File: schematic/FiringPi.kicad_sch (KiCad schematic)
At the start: 68 parts, among them IC1 HX711, J10 PT3, J11 PT4, J12 UART, J13 RTD0, J14 RTD1, J15 Pin, J3 Conn_01x03, J4 Conn_01x03, J5 Relay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

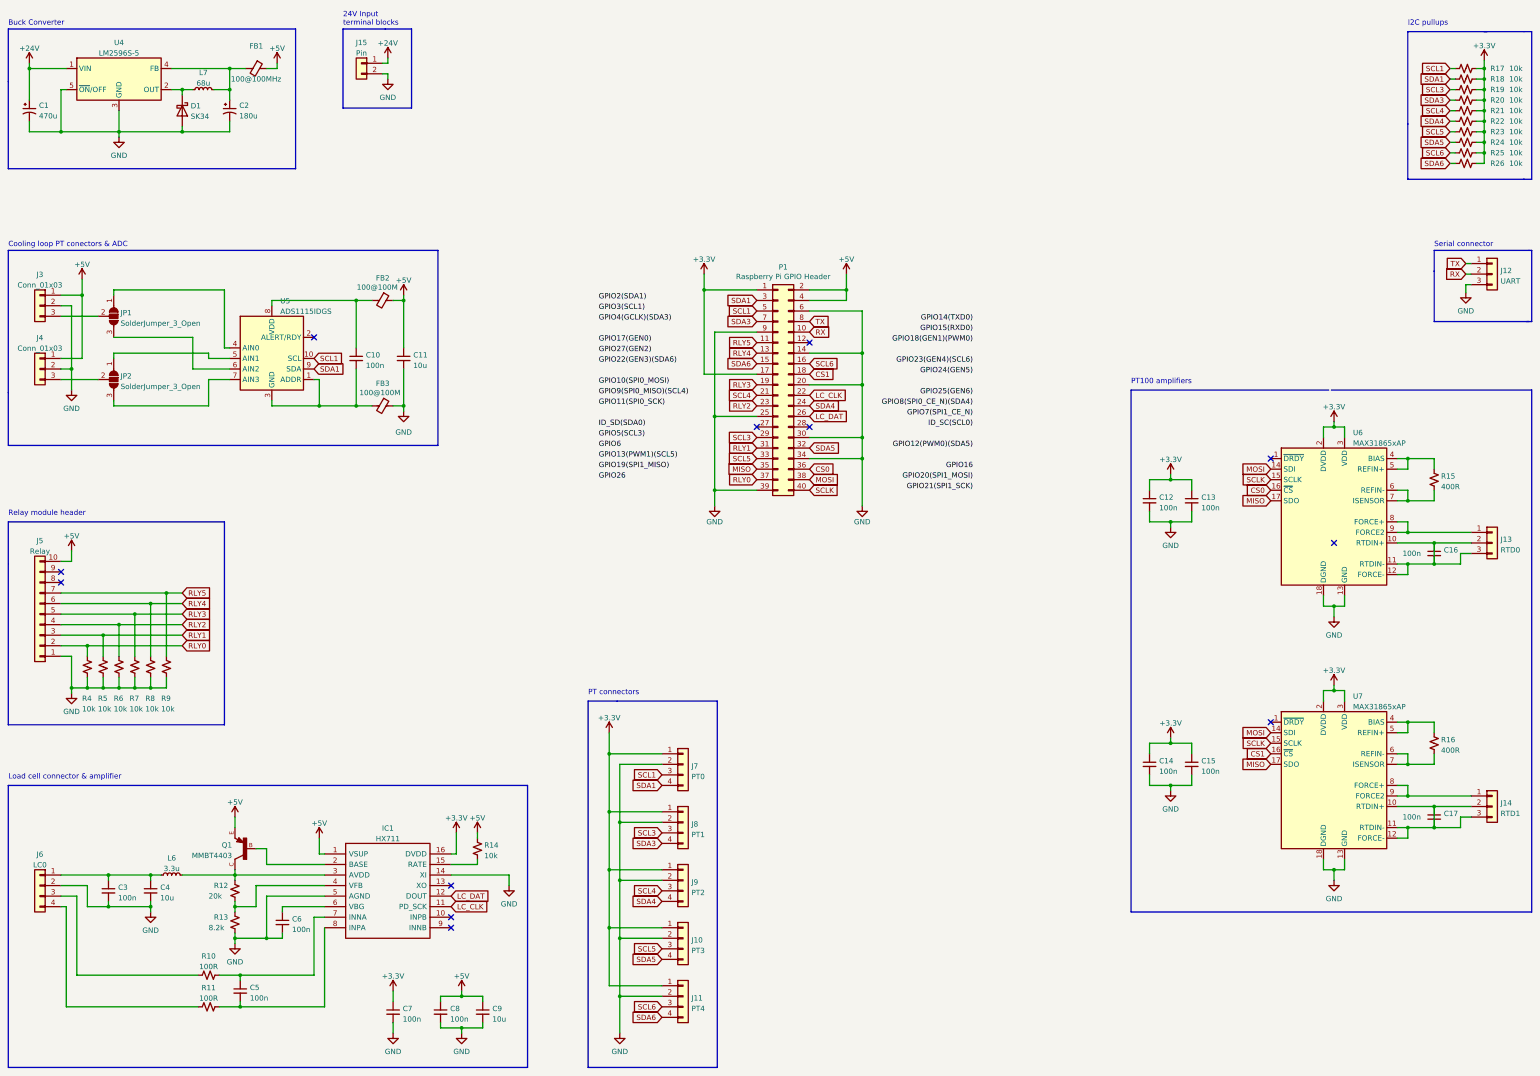
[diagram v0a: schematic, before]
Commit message: Added V2 Pi hat style PCB
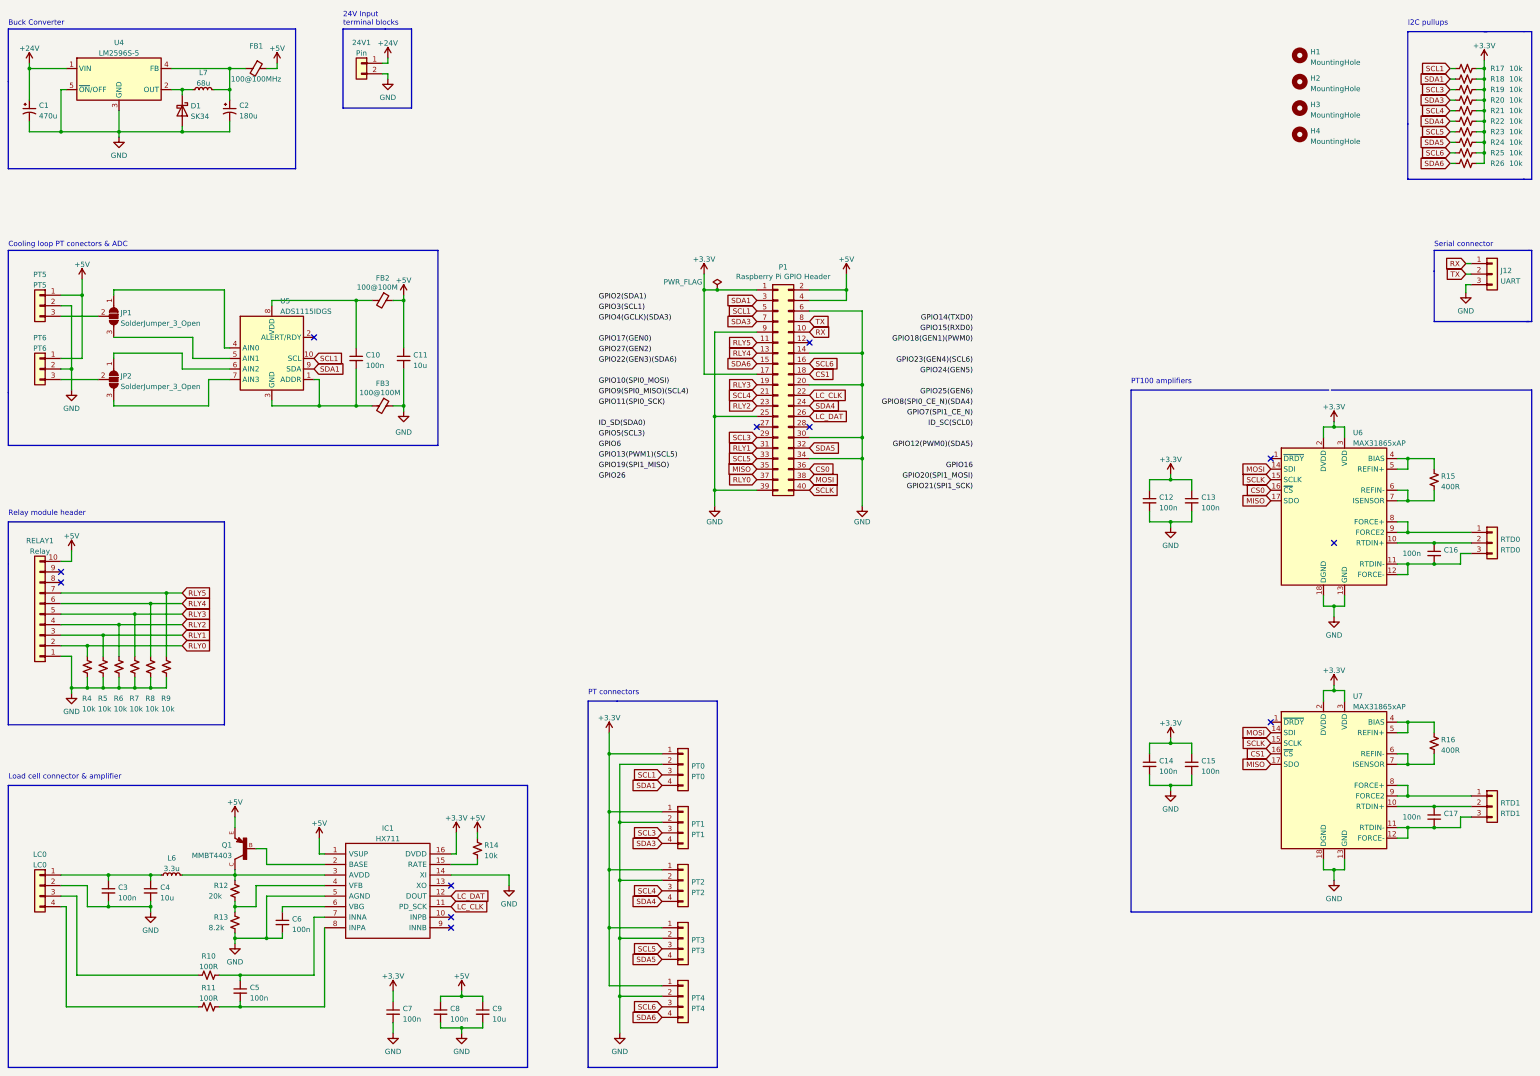
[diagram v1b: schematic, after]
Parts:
- added H1, H2, H3, H4: MountingHole, MountingHole:MountingHole_2.7mm_M2.5, symbol Mechanical:MountingHole
- 24V1: renamed from J15; footprint (none) -> Connector_JST:JST_XH_B2B-XH-A_1x02_P2.50mm_Vertical
- C10, C11, C12, C13, C14, C15, C16, C17, C3, C5, C6, C7, C8, C9: footprint (none) -> Capacitor_SMD:C_0603_1608Metric
- C2: footprint (none) -> Capacitor_THT:CP_Radial_D8.0mm_P3.50mm
- C4: footprint (none) -> Capacitor_SMD:C_0805_2012Metric
- D1: footprint (none) -> Diode_SMD:D_SMC
- FB1, FB2, FB3: footprint (none) -> Inductor_SMD:L_0805_2012Metric
- J12: footprint (none) -> Connector_JST:JST_XH_B3B-XH-A_1x03_P2.50mm_Vertical
- JP1, JP2: footprint (none) -> Jumper:SolderJumper-3_P1.3mm_Open_RoundedPad1.0x1.5mm
- L6: footprint (none) -> Inductor_SMD:L_0603_1608Metric
- L7: footprint (none) -> PE-54038SNL:PE-54038SNL
- LC0: renamed from J6; footprint (none) -> Connector_JST:JST_XH_B4B-XH-A_1x04_P2.50mm_Vertical
- PT0: renamed from J7; footprint (none) -> Connector_JST:JST_XH_B4B-XH-A_1x04_P2.50mm_Vertical
- PT1: renamed from J8; footprint (none) -> Connector_JST:JST_XH_B4B-XH-A_1x04_P2.50mm_Vertical
- PT2: renamed from J9; footprint (none) -> Connector_JST:JST_XH_B4B-XH-A_1x04_P2.50mm_Vertical
- PT3: renamed from J10; footprint (none) -> Connector_JST:JST_XH_B4B-XH-A_1x04_P2.50mm_Vertical
- PT4: renamed from J11; footprint (none) -> Connector_JST:JST_XH_B4B-XH-A_1x04_P2.50mm_Vertical
- PT5: renamed from J3; value Conn_01x03 -> PT5; footprint (none) -> Connector_JST:JST_XH_B3B-XH-A_1x03_P2.50mm_Vertical
- PT6: renamed from J4; value Conn_01x03 -> PT6; footprint (none) -> Connector_JST:JST_XH_B3B-XH-A_1x03_P2.50mm_Vertical
- Q1: footprint SOT23-BEC -> MMBT4403:SOT23-BEC
- R10, R11, R12, R13, R14, R15, R16, R17, R18, R19, R20, R21, R22, R23, R24, R25, R26, R4, R5, R6, R7, R8, R9: footprint (none) -> Resistor_SMD:R_0603_1608Metric
- RELAY1: renamed from J5; footprint (none) -> Connector_PinHeader_2.54mm:PinHeader_1x10_P2.54mm_Vertical
- RTD0: renamed from J13; footprint (none) -> Connector_JST:JST_XH_B3B-XH-A_1x03_P2.50mm_Vertical
- RTD1: renamed from J14; footprint (none) -> Connector_JST:JST_XH_B3B-XH-A_1x03_P2.50mm_Vertical
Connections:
- net +3V3 is gone; now on net +3.3V: P1.1 (Pin_1), P1.17 (Pin_17)
- net RX: now also J12.1 (Pin_1); no longer J12.2 (Pin_2)
- net TX: now also J12.2 (Pin_2); no longer J12.1 (Pin_1)
- net at C17.2, RTD1.3 (Pin_3), U7.11 (RTDIN-)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: no longer C17.1, RTD1.2 (Pin_2), U7.10 (RTDIN+)
- net at JP1.3 (B): now also U5.5 (AIN1); no longer U5.6 (AIN2)
- net at C16.2, RTD0.3 (Pin_3), U6.11 (RTDIN-)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: no longer C16.1, RTD0.2 (Pin_2), U6.10 (RTDIN+)
- net at JP2.1 (A): now also U5.6 (AIN2); no longer U5.5 (AIN1)
- new net: C17.1, RTD1.2 (Pin_2), U7.10 (RTDIN+)
- new net: C16.1, RTD0.2 (Pin_2), U6.10 (RTDIN+)

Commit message: Small tweaks
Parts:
- added D2: LED_Small, LED_SMD:LED_0805_2012Metric, symbol Device:LED_Small
- added R1: 330, Resistor_SMD:R_0603_1608Metric, symbol Device:R_Small_US
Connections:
- net GND: now also D2.1 (K)
- net at C2.1, FB1.2, L7.2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: now also R1.1
- new net: D2.2 (A), R1.2
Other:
- moved on the sheet: 24V1, FB1

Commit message: Generated gerbers
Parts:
- C4: footprint Capacitor_SMD:C_0805_2012Metric -> Capacitor_SMD:C_0603_1608Metric
- R15, R16: value 400R -> 430R
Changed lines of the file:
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@@
       (effects (font (size 1.27 1.27)) (justify left))
     )
-    (property "Value" "400R" (id 1) (at 370.586 135.6872 0)
+    (property "Value" "430R" (id 1) (at 370.586 135.6872 0)
       (effects (font (size 1.27 1.27)) (justify left))
     )
@@
       (effects (font (size 1.27 1.27)) (justify left))
     )
-    (property "Value" "400R" (id 1) (at 370.586 199.1872 0)
+    (property "Value" "430R" (id 1) (at 370.586 199.1872 0)
       (effects (font (size 1.27 1.27)) (justify left))
     )
@@
       (effects (font (size 1.27 1.27)) (justify left))
     )
-    (property "Footprint" "Capacitor_SMD:C_0805_2012Metric" (id 2) (at 59.69 233.045 0)
+    (property "Footprint" "Capacitor_SMD:C_0603_1608Metric" (id 2) (at 59.69 233.045 0)
       (effects (font (size 1.27 1.27)) hide)
     )
@@
     )
     (path "/b894b86d-6e34-4772-9865-998f9ce03312"
-      (reference "C4") (unit 1) (value "10u") (footprint "Capacitor_SMD:C_0805_2012Metric")
+      (reference "C4") (unit 1) (value "10u") (footprint "Capacitor_SMD:C_0603_1608Metric")
     )
     (path "/b3bcc8e3-5bf0-4afc-8b06-0bf5e285ff36"
@@
     )
     (path "/144c7872-6df8-48e2-9e72-dab5128a4fa7"
-      (reference "R15") (unit 1) (value "400R") (footprint "Resistor_SMD:R_0603_1608Metric")
+      (reference "R15") (unit 1) (value "430R") (footprint "Resistor_SMD:R_0603_1608Metric")
     )
     (path "/29640681-c3df-41d7-b0d0-925ecb8db18e"
-      (reference "R16") (unit 1) (value "400R") (footprint "Resistor_SMD:R_0603_1608Metric")
+      (reference "R16") (unit 1) (value "430R") (footprint "Resistor_SMD:R_0603_1608Metric")
     )
     (path "/c4172d89-4355-49d4-91b2-3c9127c62b8f"
